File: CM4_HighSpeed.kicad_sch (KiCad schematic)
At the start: 5 parts, among them J6 Conn_01x22_Female, J7 Conn_01x22_Female

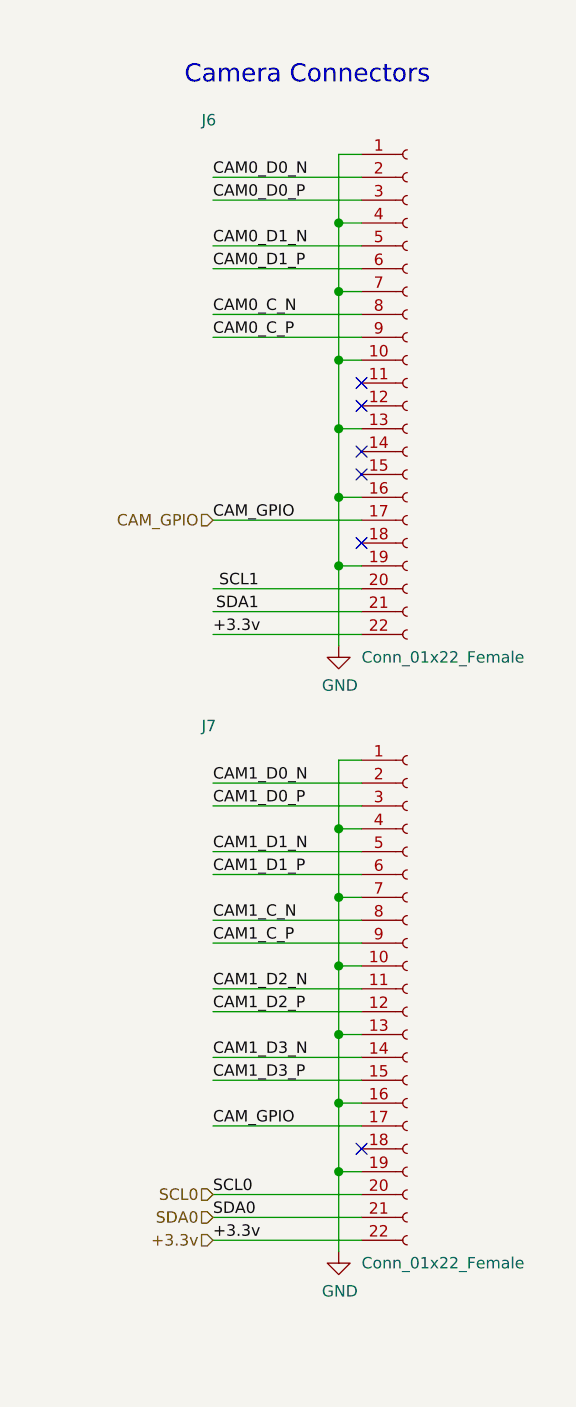
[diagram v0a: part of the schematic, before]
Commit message: added components for new DC/DC regulator
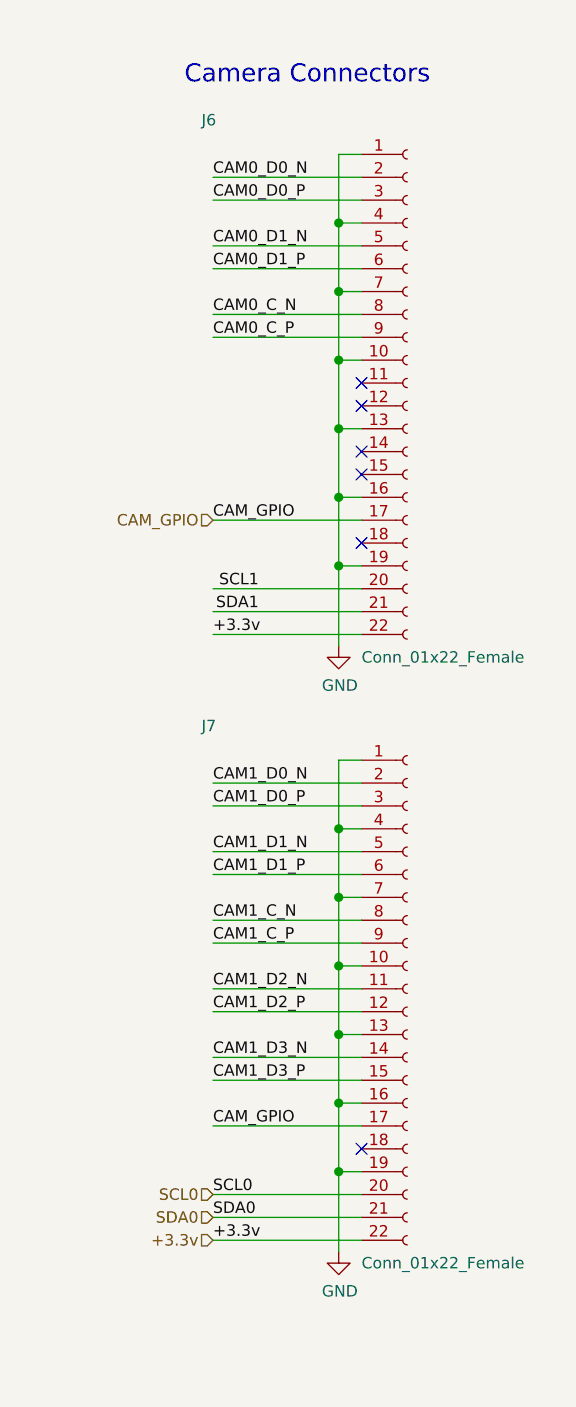
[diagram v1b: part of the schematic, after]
